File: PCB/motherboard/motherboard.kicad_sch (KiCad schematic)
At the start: 0 parts

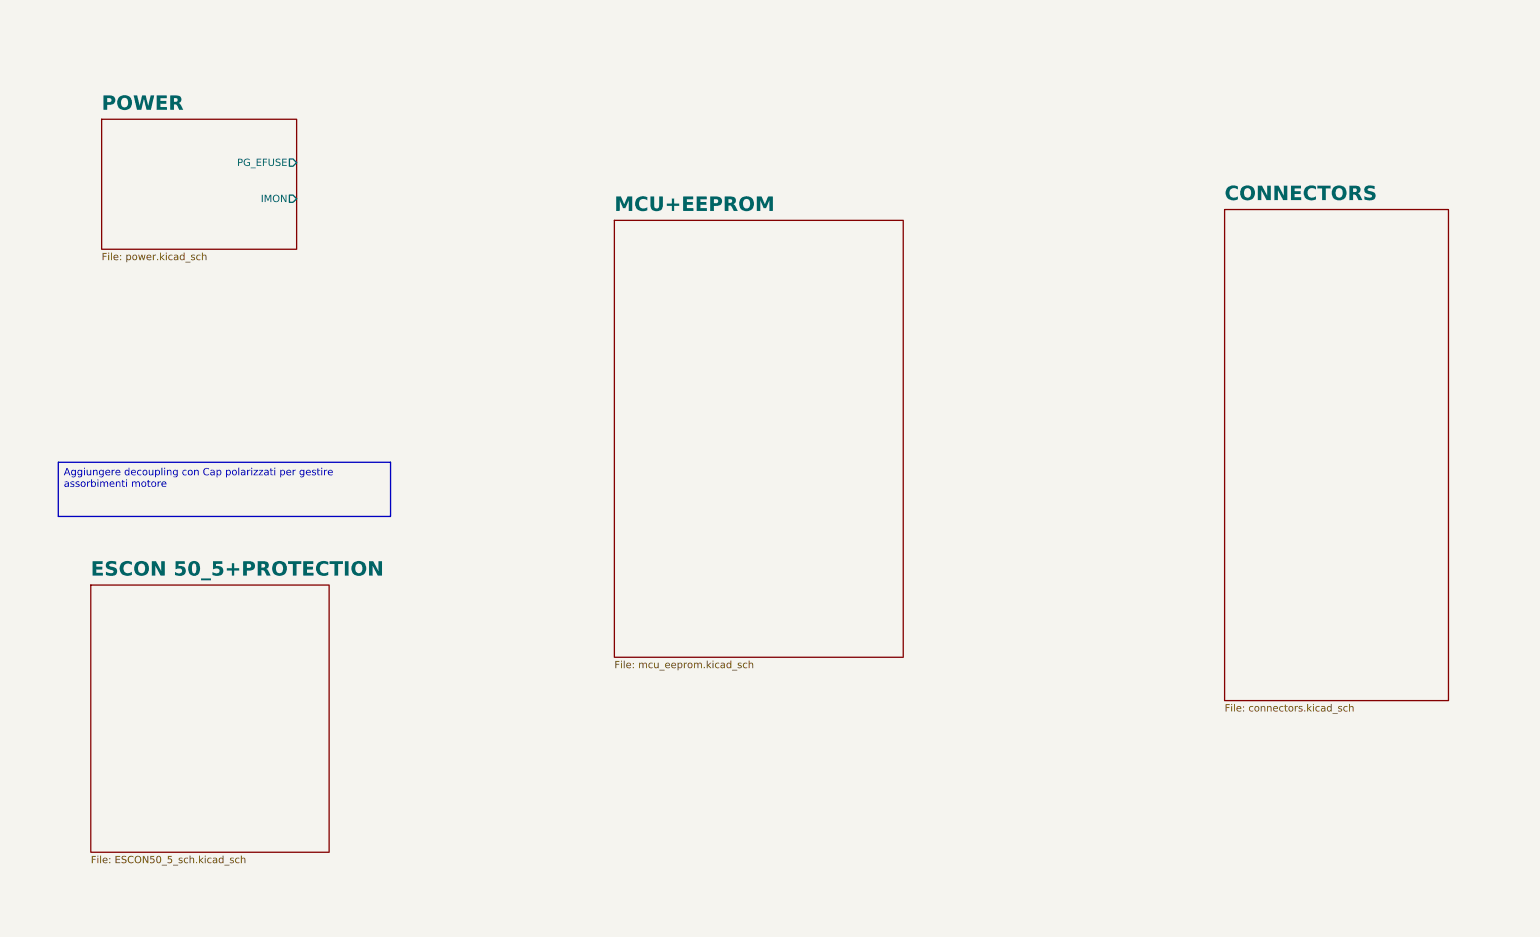
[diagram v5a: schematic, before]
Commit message: collegamenti tra blocchi schematico, sistemati connettori,finita la parte di shunt monitor per back EMF escon, aggiunti status LED, aggiunti bulk cap su alimentazione+altre modifiche
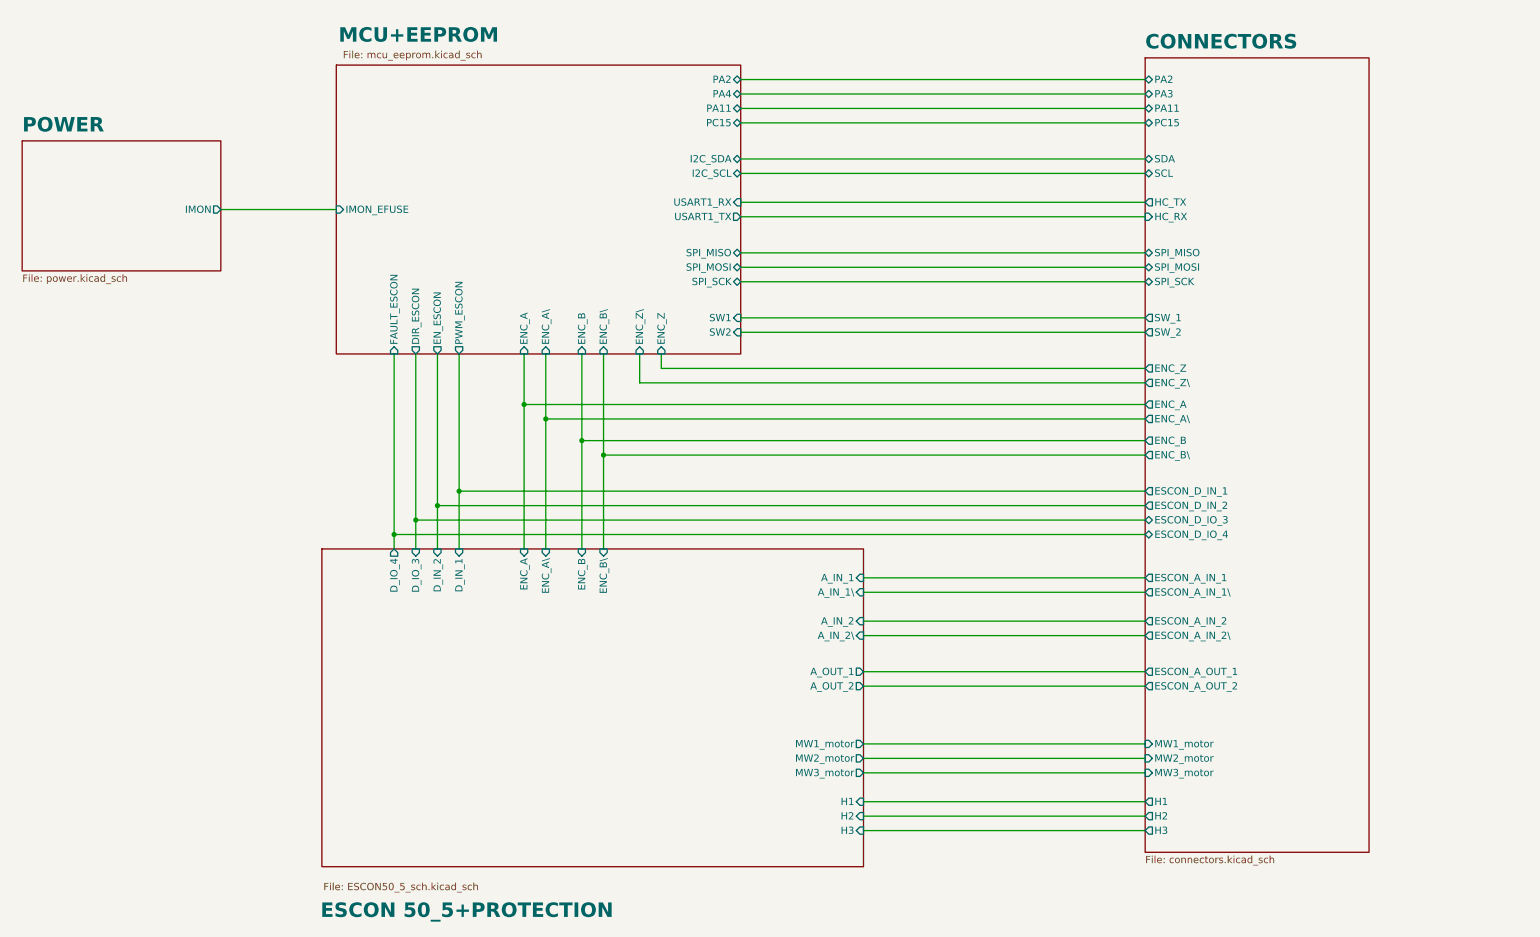
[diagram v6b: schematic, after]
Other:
- sheet CONNECTORS ports: added ENC_A, ENC_A\, ENC_B, ENC_B\, ENC_Z, ENC_Z\, ESCON_A_IN_1, ESCON_A_IN_1\, ESCON_A_IN_2, ESCON_A_IN_2\, ESCON_A_OUT_1, ESCON_A_OUT_2, ESCON_D_IN_1, ESCON_D_IN_2, ESCON_D_IO_3, ESCON_D_IO_4, H1, H2, H3, HC_RX, HC_TX, MW1_motor, MW2_motor, MW3_motor, PA11, PA2, PA3, PC15, SCL, SDA, SPI_MISO, SPI_MOSI, SPI_SCK, SW_1, SW_2; removed none
- sheet ESCON 50_5+PROTECTION ports: added A_IN_1, A_IN_1\, A_IN_2, A_IN_2\, A_OUT_1, A_OUT_2, D_IN_1, D_IN_2, D_IO_3, D_IO_4, ENC_A, ENC_A\, ENC_B, ENC_B\, H1, H2, H3, MW1_motor, MW2_motor, MW3_motor; removed none
- sheet MCU+EEPROM ports: added DIR_ESCON, ENC_A, ENC_A\, ENC_B, ENC_B\, ENC_Z, ENC_Z\, EN_ESCON, FAULT_ESCON, I2C_SCL, I2C_SDA, IMON_EFUSE, PA11, PA2, PA4, PC15, PWM_ESCON, SPI_MISO, SPI_MOSI, SPI_SCK, SW1, SW2, USART1_RX, USART1_TX; removed none
- sheet POWER ports: added none; removed PG_EFUSE

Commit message: schematics need only sizing
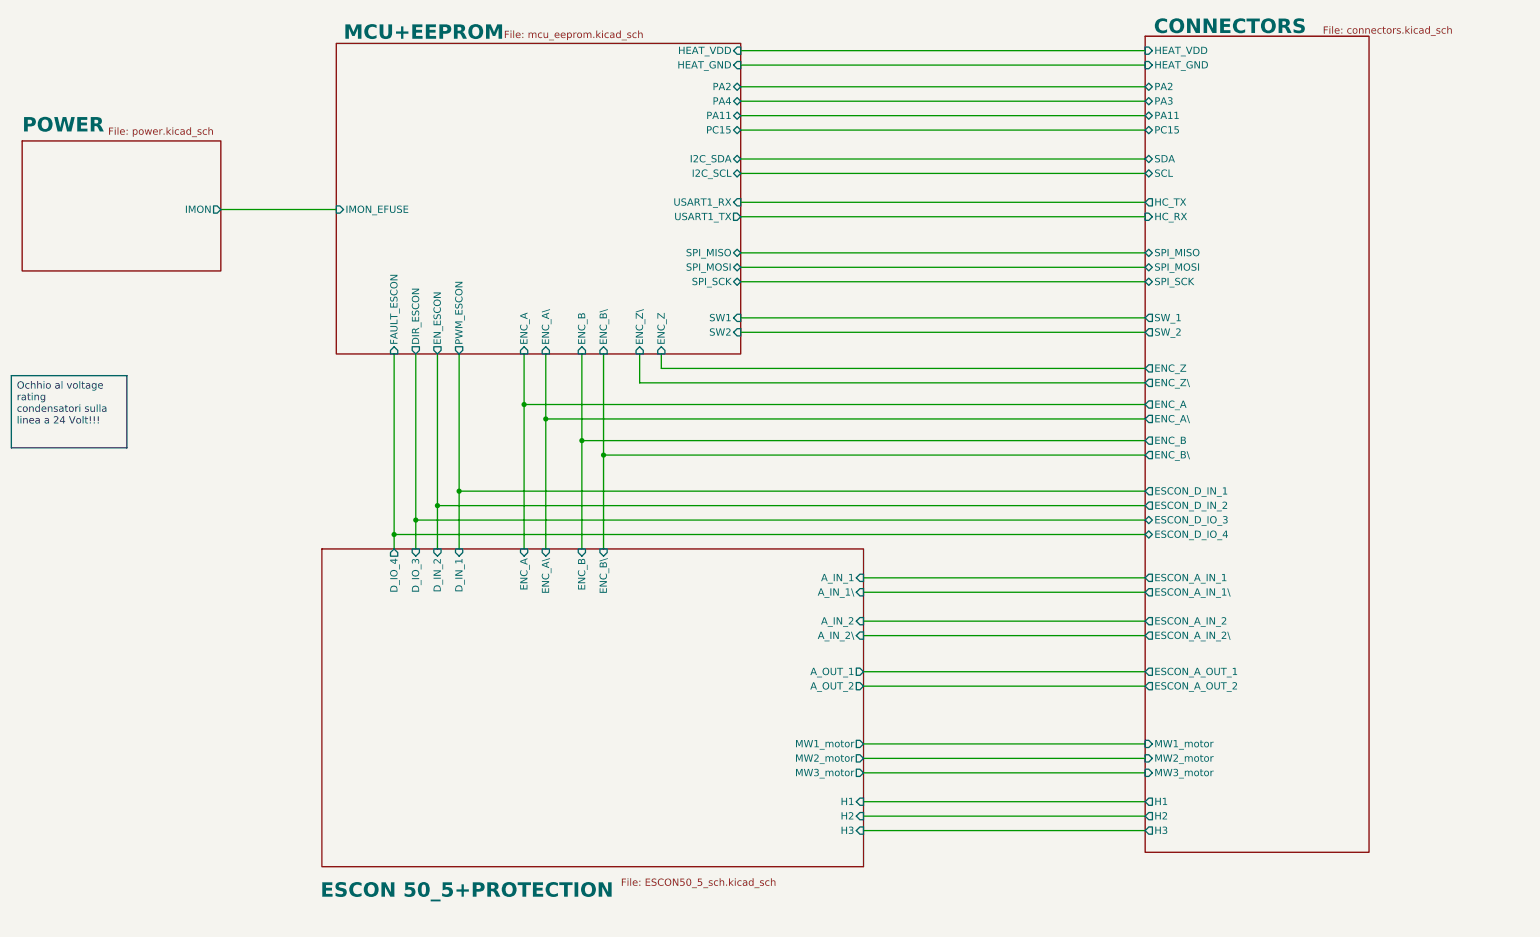
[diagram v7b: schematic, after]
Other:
- sheet CONNECTORS ports: added HEAT_GND, HEAT_VDD; removed none
- sheet MCU+EEPROM ports: added HEAT_GND, HEAT_VDD; removed none
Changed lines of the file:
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@@
 		(rev "0")
+	)
+	(text_box "Ochhio al voltage rating condensatori sulla linea a 24 Volt!!!\n"
+		(exclude_from_sim no)
+		(at 13.97 76.2 0)
+		(size 20.32 12.7)
+		(margins 0.9525 0.9525 0.9525 0.9525)
+		(stroke
+			(width 0)
+			(type solid)
+		)
+		(fill
+			(type none)
+		)
+		(effects
+			(font
+				(size 1.27 1.27)
+			)
+			(justify left top)
+		)
+	)
+	(junction
+		(at 118.11 90.17)
+		(diameter 0)
+		(color 0 0 0 0)
+	)
+	(junction
+		(at 85.09 101.6)
+		(diameter 0)
+		(color 0 0 0 0)
+	)
+	(junction
+		(at 107.95 83.82)
+		(diameter 0)
+		(color 0 0 0 0)
+	)
+	(junction
+		(at 104.14 81.28)
+		(diameter 0)
+		(color 0 0 0 0)
+	)
+	(junction
+		(at 114.3 87.63)
+		(diameter 0)
+		(color 0 0 0 0)
+	)
+	(junction
+		(at 88.9 99.06)
+		(diameter 0)
+		(color 0 0 0 0)
 	)
 	(junction
@@
 	)
 	(junction
-		(at 118.11 90.17)
-		(diameter 0)
-		(color 0 0 0 0)
-	)
-	(junction
-		(at 114.3 87.63)
-		(diameter 0)
-		(color 0 0 0 0)
-	)
-	(junction
 		(at 81.28 104.14)
 		(diameter 0)
 		(color 0 0 0 0)
 	)
-	(junction
-		(at 107.95 83.82)
-		(diameter 0)
-		(color 0 0 0 0)
-	)
-	(junction
-		(at 85.09 101.6)
-		(diameter 0)
-		(color 0 0 0 0)
-	)
-	(junction
-		(at 104.14 81.28)
-		(diameter 0)
-		(color 0 0 0 0)
-	)
-	(junction
-		(at 88.9 99.06)
-		(diameter 0)
-		(color 0 0 0 0)
-	)
 	(wire
 		(pts
@@
 	(wire
 		(pts
+			(xy 142.24 21.59) (xy 213.36 21.59)
+		)
+		(stroke
+			(width 0)
+			(type default)
+		)
+	)
+	(wire
+		(pts
 			(xy 107.95 72.39) (xy 107.95 83.82)
 		)
@@
 	(wire
 		(pts
-			(xy 142.24 24.13) (xy 213.36 24.13)
+			(xy 142.24 25.4) (xy 213.36 25.4)
 		)
 		(stroke
@@
 	(wire
 		(pts
-			(xy 142.24 31.75) (xy 213.36 31.75)
+			(xy 142.24 33.02) (xy 213.36 33.02)
 		)
 		(stroke
@@
 	(wire
 		(pts
+			(xy 142.24 19.05) (xy 213.36 19.05)
+		)
+		(stroke
+			(width 0)
+			(type default)
+		)
+	)
+	(wire
+		(pts
 			(xy 128.27 74.93) (xy 213.36 74.93)
 		)
@@
 	(wire
 		(pts
-			(xy 142.24 29.21) (xy 213.36 29.21)
+			(xy 142.24 30.48) (xy 213.36 30.48)
 		)
 		(stroke
@@
 	(wire
 		(pts
-			(xy 142.24 26.67) (xy 213.36 26.67)
+			(xy 142.24 27.94) (xy 213.36 27.94)
 		)
 		(stroke
@@
 		)
 		(fill
-			(color 245 255 30 1)
+			(color 255 234 139 1)
 		)
 		(property "Sheetname" "ESCON 50_5+PROTECTION"
-			(at 68.326 171.704 0)
+			(at 68.326 168.148 0)
 			(show_name no)
 			(do_not_autoplace no)
@@
 		)
 		(property "Sheetfile" "ESCON50_5_sch.kicad_sch"
-			(at 68.834 165.354 0)
+			(at 121.158 164.592 0)
 			(show_name no)
 			(do_not_autoplace no)
@@
 	)
 	(sheet
-		(at 213.36 20.32)
-		(size 39.37 139.7)
+		(at 213.36 16.51)
+		(size 39.37 143.51)
 		(exclude_from_sim no)
 		(in_bom yes)
 		(on_board yes)
 		(dnp no)
-		(fields_autoplaced yes)
 		(stroke
 			(width 0.1524)
@@
 		)
 		(fill
-			(color 39 240 255 1)
+			(color 119 255 193 1)
 		)
 		(property "Sheetname" "CONNECTORS"
-			(at 213.36 18.9734 0)
+			(at 214.884 16.256 0)
 			(show_name no)
 			(do_not_autoplace no)
@@
 		)
 		(property "Sheetfile" "connectors.kicad_sch"
-			(at 213.36 160.6046 0)
+			(at 244.602 14.732 0)
 			(show_name no)
 			(do_not_autoplace no)
@@
 		)
 		(pin "PC15" bidirectional
-			(at 213.36 31.75 180)
+			(at 213.36 33.02 180)
 			(effects
 				(font
@@
 		)
 		(pin "PA3" bidirectional
-			(at 213.36 26.67 180)
+			(at 213.36 27.94 180)
 			(effects
 				(font
@@
 		)
 		(pin "PA11" bidirectional
-			(at 213.36 29.21 180)
+			(at 213.36 30.48 180)
 			(effects
 				(font
@@
 		)
 		(pin "PA2" bidirectional
-			(at 213.36 24.13 180)
+			(at 213.36 25.4 180)
+			(effects
+				(font
+					(size 1.27 1.27)
+				)
+				(justify left)
+			)
+		)
+		(pin "HEAT_GND" input
+			(at 213.36 21.59 180)
+			(effects
+				(font
+					(size 1.27 1.27)
+				)
+				(justify left)
+			)
+		)
+		(pin "HEAT_VDD" input
+			(at 213.36 19.05 180)
 			(effects
 				(font
@@
 	)
 	(sheet
-		(at 71.12 21.59)
-		(size 71.12 50.8)
+		(at 71.12 17.78)
+		(size 71.12 54.61)
 		(exclude_from_sim no)
 		(in_bom yes)
@@
 		)
 		(fill
-			(color 244 113 255 1)
+			(color 217 52 255 1)
 		)
 		(property "Sheetname" "MCU+EEPROM"
-			(at 71.501 17.78 0)
+			(at 72.39 17.272 0)
 			(show_name no)
 			(do_not_autoplace no)
@@
 		)
 		(property "Sheetfile" "mcu_eeprom.kicad_sch"
-			(at 72.263 19.05 0)
+			(at 100.584 15.494 0)
 			(show_name no)
 			(do_not_autoplace no)
@@
 		)
 		(pin "PA4" bidirectional
-			(at 142.24 26.67 0)
+			(at 142.24 27.94 0)
 			(effects
 				(font
@@
 		)
 		(pin "PA11" bidirectional
-			(at 142.24 29.21 0)
+			(at 142.24 30.48 0)
 			(effects
 				(font
@@
 		)
 		(pin "PC15" bidirectional
-			(at 142.24 31.75 0)
+			(at 142.24 33.02 0)
 			(effects
 				(font
@@
 		)
 		(pin "PA2" bidirectional
-			(at 142.24 24.13 0)
+			(at 142.24 25.4 0)
+			(effects
+				(font
+					(size 1.27 1.27)
+				)
+				(justify right)
+			)
+		)
+		(pin "HEAT_GND" input
+			(at 142.24 21.59 0)
+			(effects
+				(font
+					(size 1.27 1.27)
+				)
+				(justify right)
+			)
+		)
+		(pin "HEAT_VDD" input
+			(at 142.24 19.05 0)
 			(effects
 				(font
@@
 		(on_board yes)
 		(dnp no)
-		(fields_autoplaced yes)
 		(stroke
 			(width 0.1524)
@@
 		)
 		(fill
-			(color 255 171 19 1)
+			(color 255 85 87 1)
 		)
 		(property "Sheetname" "POWER"
@@
 		)
 		(property "Sheetfile" "power.kicad_sch"
-			(at 15.875 58.3696 0)
+			(at 30.988 32.512 0)
 			(show_name no)
 			(do_not_autoplace no)

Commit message: sizing schematics done
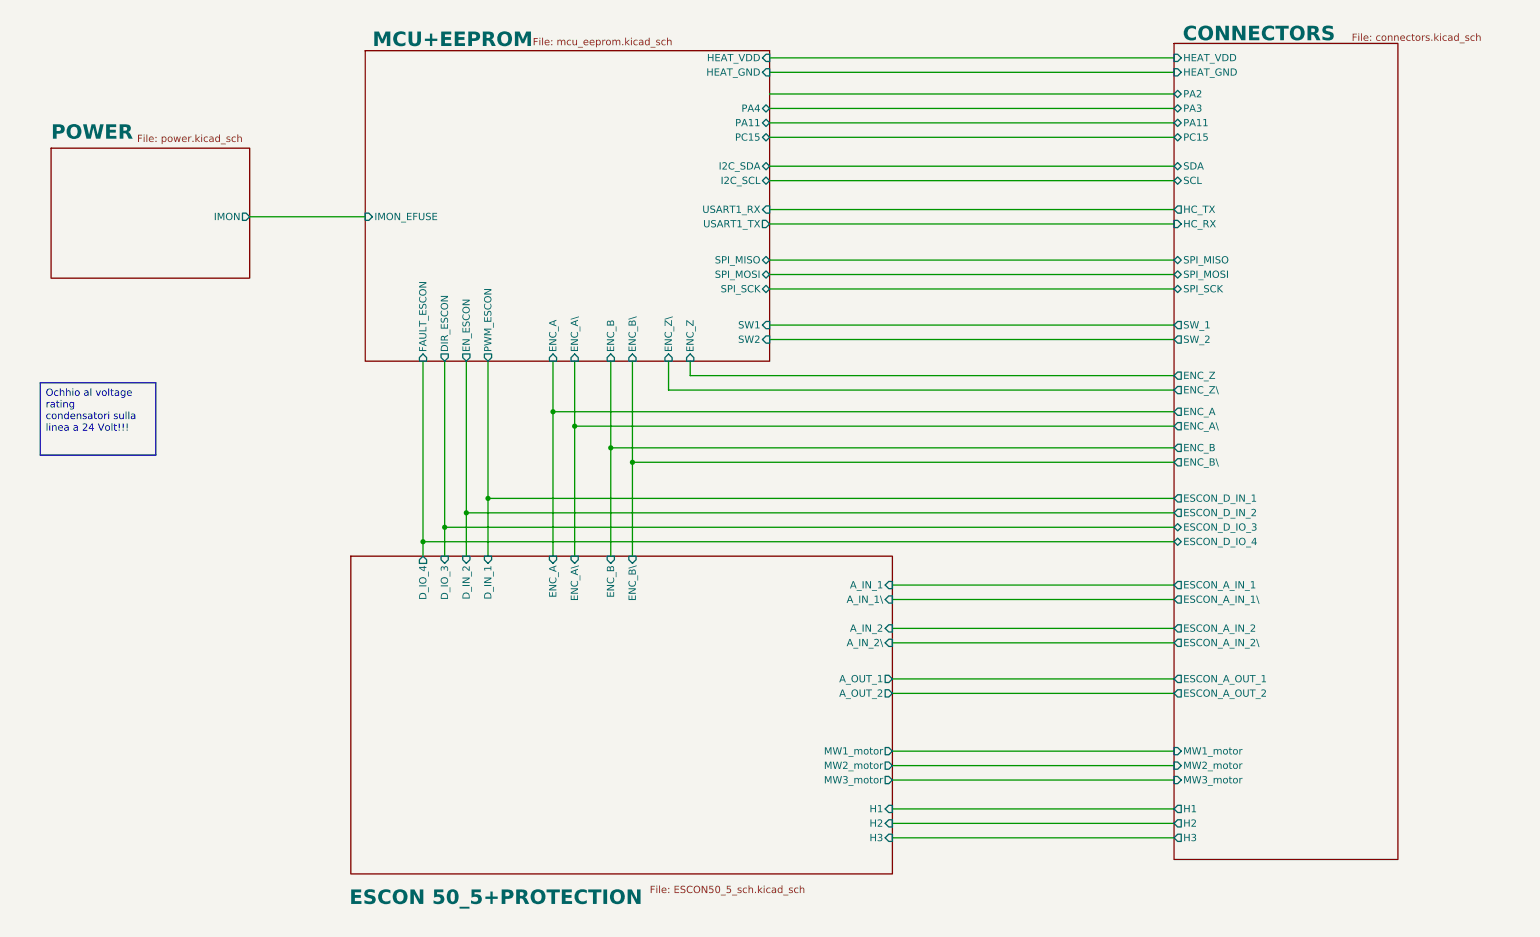
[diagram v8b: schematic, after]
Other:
- sheet MCU+EEPROM ports: added none; removed PA2
